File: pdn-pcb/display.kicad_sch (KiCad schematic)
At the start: 35 parts, among them U6 Display

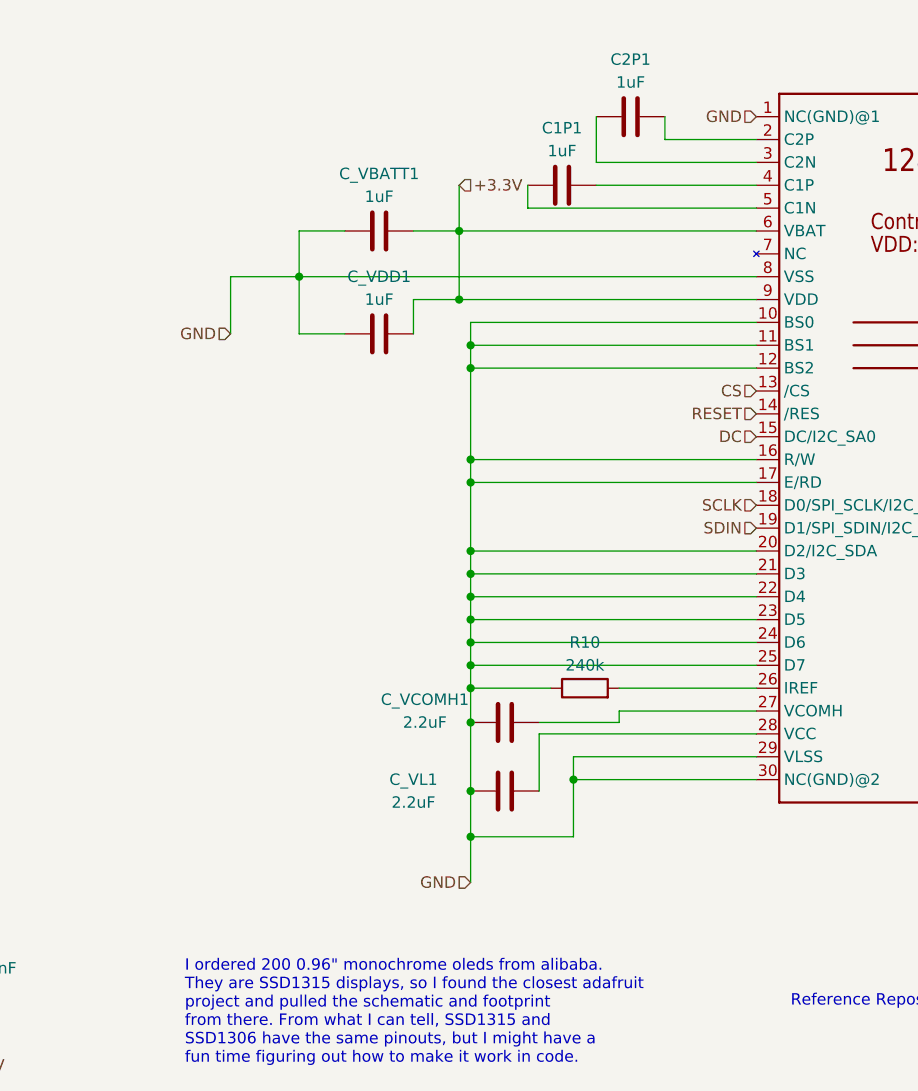
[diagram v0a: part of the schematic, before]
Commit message: Updated display, user board and display board.
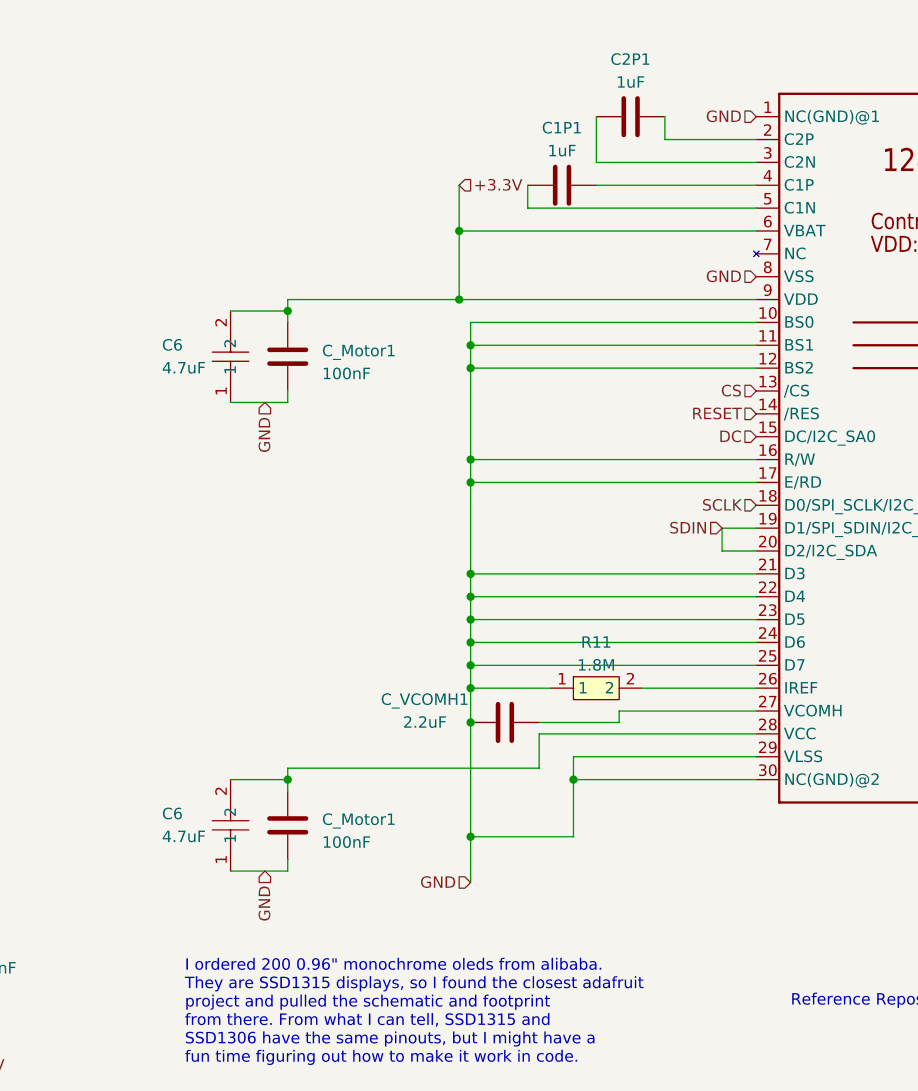
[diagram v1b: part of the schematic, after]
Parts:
- removed C_VBATT1, C_VDD1: 1uF, global:C0805, symbol Device:C
- removed C_VL1: 2.2uF, global:C0402, symbol Device:C
- removed R10: 240k, Resistor_SMD:R_0805_2012Metric, symbol Device:R
- added C6 (x2): 4.7uF, global:C0805, symbol global:0805X475K160NT_C274245
- added C_Motor1 (x2): 100nF, global:C0402, symbol Device:C
- added R11: 1.8M, global:R0201, symbol global:0201WMF1824TEE
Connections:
- net +3.3V: now also C6.2, C_Motor1.2
- net GND: now also C6.1, C6.1, C_Motor1.1, C_Motor1.1, R11.1; no longer U6.20 (D2/I2C_SDA)
- net SDIN: now also U6.20 (D2/I2C_SDA)
- net at U6.28 (VCC): now also C6.2, C_Motor1.2
- net at U6.26 (IREF): now also R11.2
